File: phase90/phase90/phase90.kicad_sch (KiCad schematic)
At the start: 42 parts, among them J1 Conn_02x08_Counter_Clockwise, Q1 Q_NJFET_DSG, Q2 Q_NJFET_DSG, Q3 Q_NJFET_DSG, Q4 Q_NJFET_DSG, U10 TL071HIDBVR, U11 TL071HIDBVR, U7 TL071HIDBVR, U8 TL071HIDBVR, U9 TL071HIDBVR

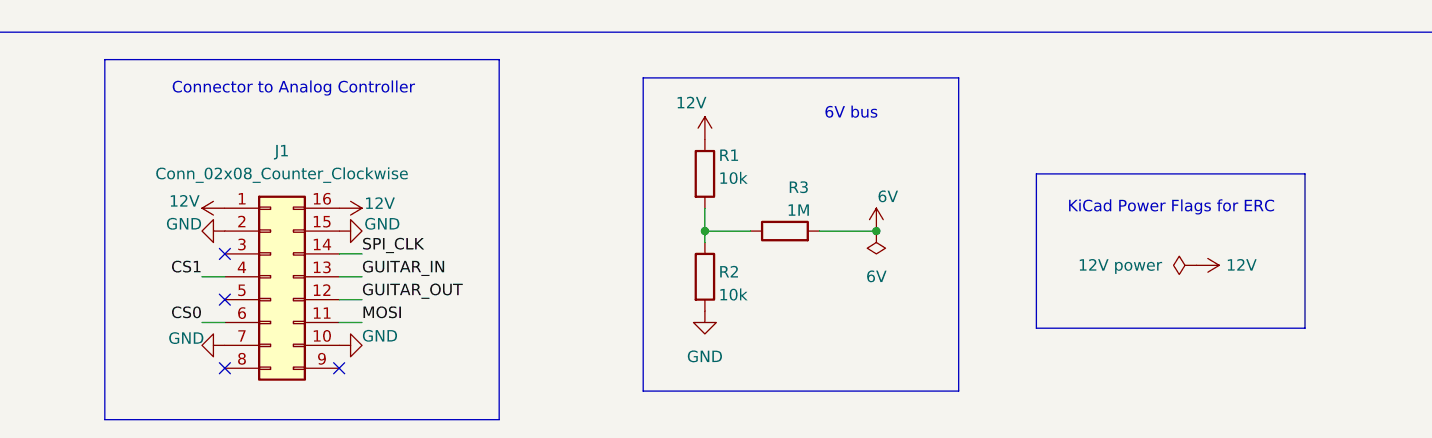
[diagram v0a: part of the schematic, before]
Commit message: changed out potentiometer for one that can do higher analog voltages
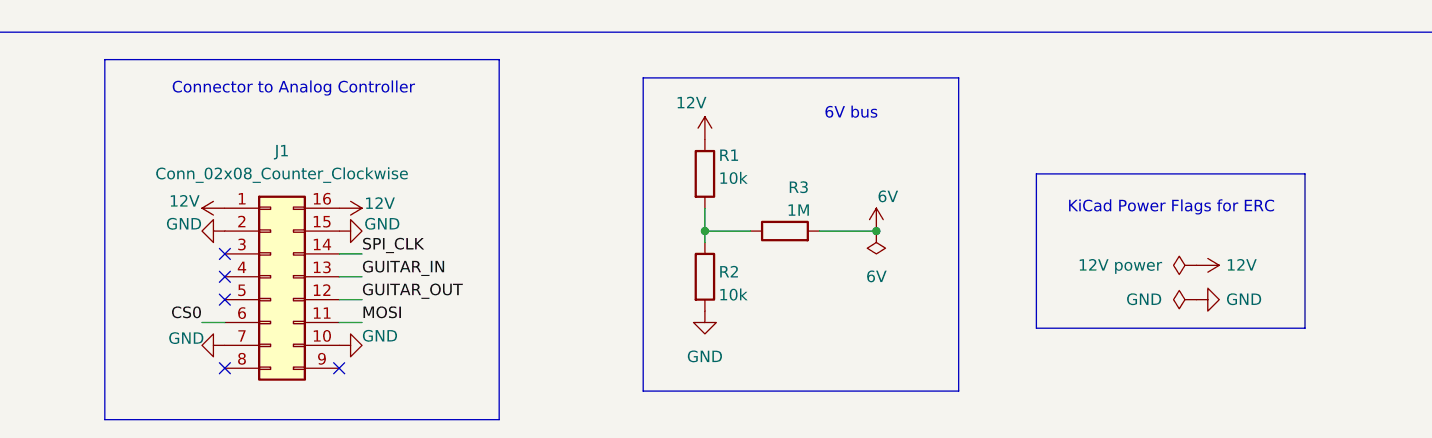
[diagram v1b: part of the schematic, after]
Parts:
- U10, U11, U7, U8, U9: footprint SOT23_DBV_5_TEX -> Package_TO_SOT_SMD:SOT-23-5
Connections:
- net CS1: no longer names the net of J1.4 (Pin_4)
- no-connect marks 4 -> 5
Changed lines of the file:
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@@
 	)
 	(no_connect
+		(at 45.72 177.8)
+	)
+	(no_connect
 		(at 45.72 175.26)
 	)
@@
 	(wire
 		(pts
-			(xy 43.18 177.8) (xy 45.72 177.8)
-		)
-		(stroke
-			(width 0)
-			(type default)
-		)
-	)
-	(wire
-		(pts
 			(xy 186.69 34.29) (xy 180.34 34.29)
 		)
@@
 		)
 	)
-	(label "CS1"
-		(at 43.18 177.8 180)
-		(effects
-			(font
-				(size 1.27 1.27)
-			)
-			(justify right bottom)
-		)
-	)
 	(label "GUITAR_IN"
 		(at 22.86 48.26 180)
@@
 			)
 		)
-		(property "Footprint" "SOT23_DBV_5_TEX"
+		(property "Footprint" "Package_TO_SOT_SMD:SOT-23-5"
 			(at 68.58 50.8 0)
 			(effects
@@
 			)
 		)
-		(property "Footprint" "SOT23_DBV_5_TEX"
+		(property "Footprint" "Package_TO_SOT_SMD:SOT-23-5"
 			(at 127 52.07 0)
 			(effects
@@
 			)
 		)
-		(property "Footprint" "SOT23_DBV_5_TEX"
+		(property "Footprint" "Package_TO_SOT_SMD:SOT-23-5"
 			(at 185.42 50.8 0)
 			(effects
@@
 	)
 	(symbol
+		(lib_id "power:GND")
+		(at 153.67 180.34 90)
+		(unit 1)
+		(exclude_from_sim no)
+		(in_bom yes)
+		(on_board yes)
+		(dnp no)
+		(property "Reference" "#PWR052"
+			(at 160.02 180.34 0)
+			(effects
+				(font
+					(size 1.27 1.27)
+				)
+				(hide yes)
+			)
+		)
+		(property "Value" "GND"
+			(at 156.972 180.34 90)
+			(effects
+				(font
+					(size 1.27 1.27)
+				)
+				(justify right)
+			)
+		)
+		(property "Footprint" ""
+			(at 153.67 180.34 0)
+			(effects
+				(font
+					(size 1.27 1.27)
+				)
+				(hide yes)
+			)
+		)
+		(property "Datasheet" ""
+			(at 153.67 180.34 0)
+			(effects
+				(font
+					(size 1.27 1.27)
+				)
+				(hide yes)
+			)
+		)
+		(property "Description" "Power symbol creates a global label with name \"GND\" , ground"
+			(at 153.67 180.34 0)
+			(effects
+				(font
+					(size 1.27 1.27)
+				)
+				(hide yes)
+			)
+		)
+		(pin "1"
+		)
+		(instances
+			(project "phase90"
+				(path "/68e2c4ae-e968-491c-8ad8-cd53d3f65ea8"
+					(reference "#PWR052")
+					(unit 1)
+				)
+			)
+		)
+	)
+	(symbol
 		(lib_id "TL071HIDBVR:TL071HIDBVR")
 		(at 240.03 124.46 270)
@@
 			)
 		)
-		(property "Footprint" "SOT23_DBV_5_TEX"
+		(property "Footprint" "Package_TO_SOT_SMD:SOT-23-5"
 			(at 240.03 124.46 0)
 			(effects
@@
 			)
 		)
-		(property "Footprint" "SOT23_DBV_5_TEX"
+		(property "Footprint" "Package_TO_SOT_SMD:SOT-23-5"
 			(at 243.84 50.8 0)
 			(effects
@@
 					(unit 1)
 				)
+			)
+		)
+	)
+	(symbol
+		(lib_id "power:PWR_FLAG")
+		(at 153.67 180.34 90)
+		(unit 1)
+		(exclude_from_sim no)
+		(in_bom yes)
+		(on_board yes)
+		(dnp no)
+		(fields_autoplaced yes)
+		(property "Reference" "#FLG04"
+			(at 151.765 180.34 0)
+			(effects
+				(font
+					(size 1.27 1.27)
+				)
+				(hide yes)
+			)
+		)
+		(property "Value" "GND"
+			(at 149.86 180.3399 90)
+			(effects
+				(font
+					(size 1.27 1.27)
+				)
+				(justify left)
+			)
+		)
+		(property "Footprint" ""
+			(at 153.67 180.34 0)
+			(effects
+				(font
+					(size 1.27 1.27)
+				)
+				(hide yes)
+			)
+		)
+		(property "Datasheet" "~"
+			(at 153.67 180.34 0)
+			(effects
+				(font
+					(size 1.27 1.27)
+				)
+				(hide yes)
+			)
+		)
+		(property "Description" "Special symbol for telling ERC where power comes from"
+			(at 153.67 180.34 0)
+			(effects
+				(font
+					(size 1.27 1.27)
+				)
+				(hide yes)
+			)
+		)
+		(pin "1"
+		)
+		(instances
+			(project ""
+				(path "/68e2c4ae-e968-491c-8ad8-cd53d3f65ea8"
+					(reference "#FLG04")
+					(unit 1)
+				)

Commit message: finished board except for silk screen
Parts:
- removed J1: Conn_02x08_Counter_Clockwise, Connector_PinHeader_1.00mm:PinHeader_2x08_P1.00mm_Horizontal, symbol Connector_Generic:Conn_02x08_Counter_Clockwise
- added C2: 0.1u, Capacitor_SMD:C_0603_1608Metric, symbol Device:C
- added J1: Conn_02x08_Odd_Even, Connector_PinHeader_2.54mm:PinHeader_2x08_P2.54mm_Horizontal, symbol Connector_Generic:Conn_02x08_Odd_Even
- added R39, R40: 10k, Resistor_SMD:R_0603_1608Metric, symbol Device:R
- added R41: 1M, Resistor_SMD:R_0603_1608Metric, symbol Device:R
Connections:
- net 12V: now also J1.1 (Pin_1), J1.2 (Pin_2), R39.1
- net 6V: no longer R35.2, U11.3 (IN+)
- net CS0: now also J1.11 (Pin_11)
- net GND: now also J1.13 (Pin_13), J1.14 (Pin_14), J1.3 (Pin_3), J1.4 (Pin_4), R40.2
- net GUITAR_IN: now also C2.2, J1.8 (Pin_8)
- net GUITAR_OUT: now also J1.10 (Pin_10)
- net MOSI: now also J1.12 (Pin_12)
- net SPI_CLK: now also J1.6 (Pin_6)
- new net: R39.2, R40.1, R41.1
- new net: C2.1, R35.2
- new net: R41.2, U11.3 (IN+)
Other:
- moved on the sheet: C4, C5, C6, C7, C8, C9, Q1, Q2, Q3, Q4, R1, R15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

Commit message: fixed connector also?
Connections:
- net CS0: now also J1.6 (Pin_6); no longer J1.11 (Pin_11)
- net GND: now also J1.11 (Pin_11), J1.12 (Pin_12); no longer J1.3 (Pin_3), J1.4 (Pin_4)
- net GUITAR_IN: now also J1.10 (Pin_10); no longer J1.8 (Pin_8)
- net GUITAR_OUT: now also J1.9 (Pin_9); no longer J1.10 (Pin_10)
- net MOSI: now also J1.7 (Pin_7); no longer J1.12 (Pin_12)
- net SPI_CLK: now also J1.8 (Pin_8); no longer J1.6 (Pin_6)

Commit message: added buffers and caps for op-amps on effect boards
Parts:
- added C10, C11, C12, C13, C14, C3: 1u, Capacitor_SMD:C_0603_1608Metric, symbol Device:C
- added U3: TL071HIDBVR, Package_TO_SOT_SMD:SOT-23-5, symbol TL071HIDBVR:TL071HIDBVR
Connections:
- net 12V: now also C10.1, C11.1, C12.1, C13.1, C14.1, C3.1, U3.5 (V+)
- net 6V: now also U3.3 (IN+); no longer C4.1, R15.1
- net GND: now also C10.2, C11.2, C12.2, C13.2, C14.2, C3.2, U3.2 (V-)
- new net: C4.1, R15.1, U3.1 (OUT), U3.4 (IN-)
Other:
- note added: "Caps for Op-Amps"
- moved on the sheet: C5, R1, R2, R3
